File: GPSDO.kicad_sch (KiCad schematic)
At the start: 91 parts, among them J1 Conn_Coaxial, J10 PROG, J2 GPS_CONN, J3 Conn_Coaxial, J4 Conn_Coaxial, J5 Conn_Coaxial, J6 Conn_Coaxial, J7 DISP_MODULE, J8 Barrel_Jack, J9 Conn_Coaxial, SW1 RESET_BTN, U1 REF3450, U10 MC7805BDTRKG, U11 74AUC1G74, U12 74AUC2G04, U13 74AUC2G04, U14 DS34C87T, U15 MCP6486T-E/OT, U2 74LVC1G125SE-7, U3 AD5680, U4 NB3N551MN, U5 LTC2050IS8, U6 AVR32DB28x-xSO, U7 74LVC1G125SE-7, U8 74HC390, U9 L7805CV, X1 OC5SC25

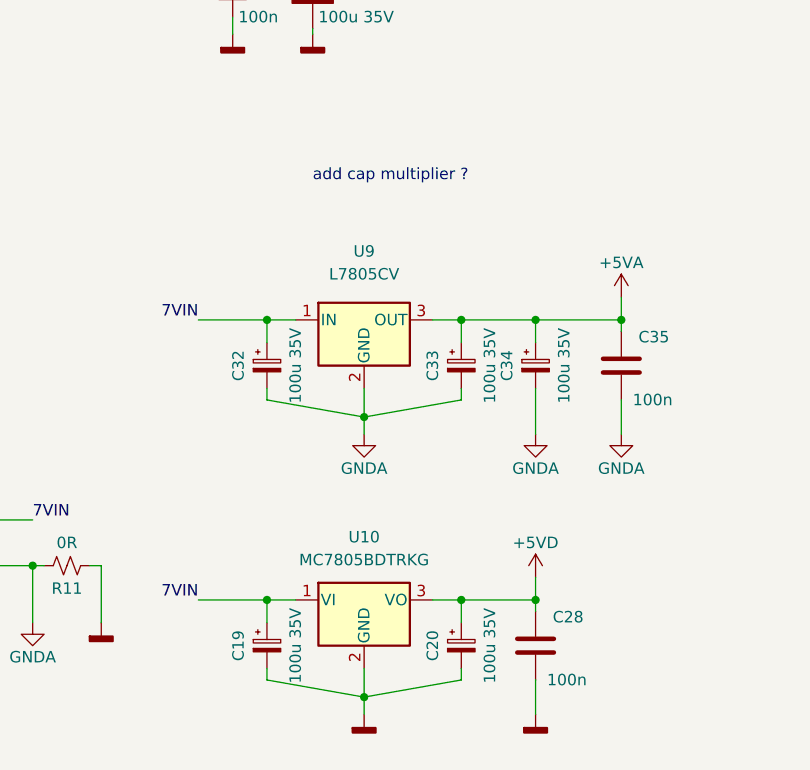
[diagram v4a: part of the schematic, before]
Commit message: LDO power supply
preliminary component choice
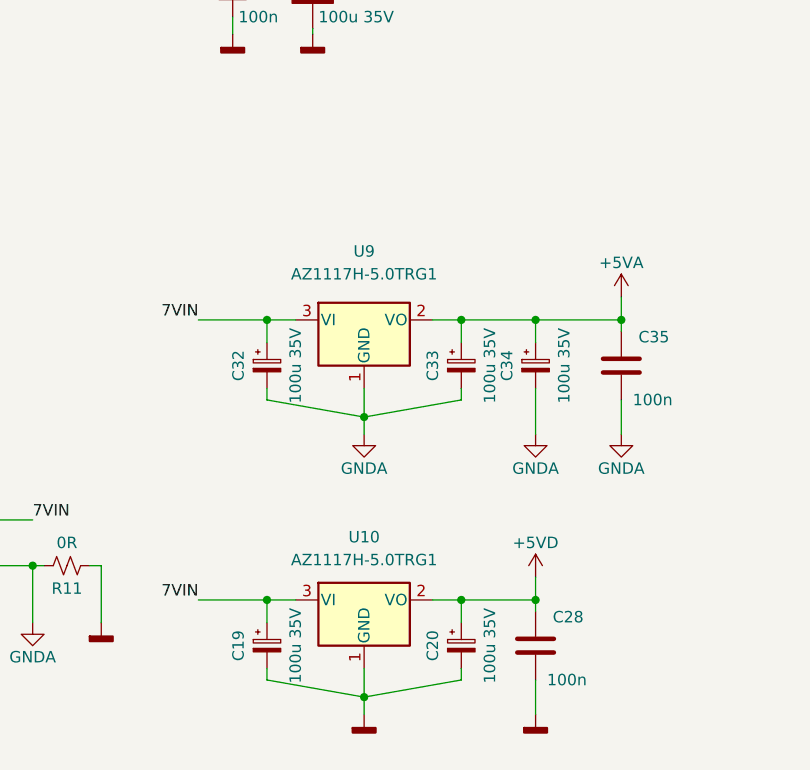
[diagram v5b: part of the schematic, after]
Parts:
- removed U10: MC7805BDTRKG, Package_TO_SOT_SMD:TO-252-2, symbol Regulator_Linear:LM78M05_TO252
- removed U9: L7805CV, Package_TO_SOT_THT:TO-220-3_Horizontal_TabDown, symbol Regulator_Linear:L7805
- added U10, U9: AZ1117H-5.0TRG1, Package_TO_SOT_SMD:SOT-223-3_TabPin2, symbol Regulator_Linear:AZ1117-5.0
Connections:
- net +5VA: now also U9.2 (VO)
- net +5VD: now also U10.2 (VO)
- net 7VIN: now also U10.3 (VI), U9.3 (VI)
- net GND: now also U10.1 (GND)
- net GNDA: now also U9.1 (GND)
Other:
- note removed: "add cap multiplier ?"
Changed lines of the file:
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@@
     (effects (font (size 1.27 1.27)) (justify left bottom))
   )
-  (text "add cap multiplier ?" (at 210.82 219.71 0)
-    (effects (font (size 1.27 1.27)) (justify left bottom))
-  )
   (text "TODO:\n - where to put trigger pin?\n - where to put ADC pin?\n-clock gen pow supply\n- check everything ok opn 5V?\n\n- (touch) display\n- serial interface\n- Main_clk_1 unused"
     (at 363.855 243.84 0)
@@
     (pin "1")
   )
-  (symbol (lib_id "Regulator_Linear:L7805") (at 216.535 234.95 0) (unit 1)
-    (in_bom yes) (on_board yes) (fields_autoplaced)
-    (property "Reference" "U9" (id 0) (at 216.535 227.33 0))
-    (property "Value" "L7805CV" (id 1) (at 216.535 229.87 0))
-    (property "Footprint" "Package_TO_SOT_THT:TO-220-3_Horizontal_TabDown" (id 2) (at 217.17 238.76 0)
-      (effects (font (size 1.27 1.27) italic) (justify left) hide)
-    )
-    (property "Datasheet" "http://www.st.com/content/ccc/resource/technical/document/datasheet/41/4f/b3/b0/12/d4/47/88/CD00000444.pdf/files/CD00000444.pdf/jcr:content/translations/en.CD00000444.pdf" (id 3) (at 216.535 236.22 0)
-      (effects (font (size 1.27 1.27)) hide)
-    )
-    (pin "1")
-    (pin "2")
-    (pin "3")
-  )
   (symbol (lib_id "power:GNDD") (at 93.345 113.03 0) (unit 1)
     (in_bom yes) (on_board yes) (fields_autoplaced)
@@
     (pin "1")
   )
+  (symbol (lib_id "Regulator_Linear:AZ1117-5.0") (at 216.535 234.95 0) (unit 1)
+    (in_bom yes) (on_board yes) (fields_autoplaced)
+    (property "Reference" "U9" (id 0) (at 216.535 227.33 0))
+    (property "Value" "AZ1117H-5.0TRG1" (id 1) (at 216.535 229.87 0))
+    (property "Footprint" "Package_TO_SOT_SMD:SOT-223-3_TabPin2" (id 2) (at 216.535 228.6 0)
+      (effects (font (size 1.27 1.27) italic) hide)
+    )
+    (property "Datasheet" "https://www.diodes.com/assets/Datasheets/AZ1117.pdf" (id 3) (at 216.535 234.95 0)
+      (effects (font (size 1.27 1.27)) hide)
+    )
+    (pin "1")
+    (pin "2")
+    (pin "3")
+  )
   (symbol (lib_id "power:GNDD") (at 53.975 273.05 0) (unit 1)
     (in_bom yes) (on_board yes) (fields_autoplaced)
@@
     (pin "2")
   )
-  (symbol (lib_id "Regulator_Linear:LM78M05_TO252") (at 216.535 266.065 0) (unit 1)
-    (in_bom yes) (on_board yes) (fields_autoplaced)
-    (property "Reference" "U10" (id 0) (at 216.535 259.08 0))
-    (property "Value" "MC7805BDTRKG" (id 1) (at 216.535 261.62 0))
-    (property "Footprint" "Package_TO_SOT_SMD:TO-252-2" (id 2) (at 216.535 260.35 0)
-      (effects (font (size 1.27 1.27) italic) hide)
-    )
-    (property "Datasheet" "https://www.onsemi.com/pub/Collateral/MC78M00-D.PDF" (id 3) (at 216.535 267.335 0)
-      (effects (font (size 1.27 1.27)) hide)
-    )
-    (pin "1")
-    (pin "2")
-    (pin "3")
-  )
   (symbol (lib_id "Device:C_Polarized") (at 20.955 267.97 0) (unit 1)
     (in_bom yes) (on_board yes)
@@
     (pin "1")
   )
+  (symbol (lib_id "Regulator_Linear:AZ1117-5.0") (at 216.535 266.065 0) (unit 1)
+    (in_bom yes) (on_board yes) (fields_autoplaced)
+    (property "Reference" "U10" (id 0) (at 216.535 259.08 0))
+    (property "Value" "AZ1117H-5.0TRG1" (id 1) (at 216.535 261.62 0))
+    (property "Footprint" "Package_TO_SOT_SMD:SOT-223-3_TabPin2" (id 2) (at 216.535 259.715 0)
+      (effects (font (size 1.27 1.27) italic) hide)
+    )
+    (property "Datasheet" "https://www.diodes.com/assets/Datasheets/AZ1117.pdf" (id 3) (at 216.535 266.065 0)
+      (effects (font (size 1.27 1.27)) hide)
+    )
+    (pin "1")
+    (pin "2")
+    (pin "3")
+  )
   (symbol (lib_id "power:+5VD") (at 44.45 262.255 0) (unit 1)
     (in_bom yes) (on_board yes) (fields_autoplaced)
@@
       (reference "U8") (unit 3) (value "74HC390") (footprint "Package_SO:SOIC-16_3.9x9.9mm_P1.27mm")
     )
-    (path "/171f434d-5c34-48ea-8f79-c330c808a2be"
-      (reference "U9") (unit 1) (value "L7805CV") (footprint "Package_TO_SOT_THT:TO-220-3_Horizontal_TabDown")
+    (path "/503e0e75-e692-4d20-8364-7dd959ad220a"
+      (reference "U9") (unit 1) (value "AZ1117H-5.0TRG1") (footprint "Package_TO_SOT_SMD:SOT-223-3_TabPin2")
     )
-    (path "/89b8a5aa-f785-4e60-9e1c-9f4b79a3f39c"
-      (reference "U10") (unit 1) (value "MC7805BDTRKG") (footprint "Package_TO_SOT_SMD:TO-252-2")
+    (path "/e6bc66eb-279a-48bf-9d76-c75432f12fc9"
+      (reference "U10") (unit 1) (value "AZ1117H-5.0TRG1") (footprint "Package_TO_SOT_SMD:SOT-223-3_TabPin2")
     )
     (path "/14b7ea0b-a3fe-410e-b47a-552eaf1c5ffd"

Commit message: minor update
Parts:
- removed C10: 100u 35V, Capacitor_SMD:C_Elec_6.3x7.7, symbol Device:C_Polarized
- added D3: LED, LED_SMD:LED_0805_2012Metric, symbol Device:LED
- added R13: 270R, Resistor_SMD:R_0805_2012Metric_Pad1.20x1.40mm_HandSolder, symbol Device:R_Small_US
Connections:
- net +5VA: now also D3.2 (A)
- net GNDA: now also R13.1
- new net: D3.1 (K), R13.2
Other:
- note added: "PD4 is the Waveform Output for TCA0"
- moved on the sheet: C31, C46, J10, J2, J9, R12, R8, R9, U11, U15, U2, U7

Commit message: intermediate solution for layout
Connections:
- net TOUCH_IRQ: now also U6.1 (PA7); no longer U6.8 (PD2)
- net ~{DAC_SS}: now also U6.8 (PD2); no longer U6.1 (PA7)
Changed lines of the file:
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@@
     (effects (font (size 1.27 1.27)) (justify right bottom))
   )
-  (label "TOUCH_IRQ" (at 151.13 111.76 0)
-    (effects (font (size 1.27 1.27)) (justify left bottom))
+  (label "TOUCH_IRQ" (at 217.805 111.76 180)
+    (effects (font (size 1.27 1.27)) (justify right bottom))
   )
   (label "~{TOUCH_SS}" (at 217.805 124.46 180)
@@
     (effects (font (size 1.27 1.27)) (justify left bottom))
   )
-  (label "~{DAC_SS}" (at 217.805 111.76 180)
-    (effects (font (size 1.27 1.27)) (justify right bottom))
+  (label "~{DAC_SS}" (at 151.13 111.76 0)
+    (effects (font (size 1.27 1.27)) (justify left bottom))
   )
   (label "TOUCH_MISO" (at 231.775 119.38 180)

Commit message: first routing
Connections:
- net GND: now also R11.2; no longer R11.1
- net GNDA: now also R11.1; no longer R11.2
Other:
- note added: "DAC and LCD Touch share SPI iface"
- moved on the sheet: R11
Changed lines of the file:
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@@
+    (effects (font (size 1.27 1.27)) (justify left bottom))
+  )
+  (text "DAC and LCD Touch share\nSPI iface" (at 243.84 120.65 0)
     (effects (font (size 1.27 1.27)) (justify left bottom))
   )
@@
     (pin "1")
   )
-  (symbol (lib_id "Device:R_Small_US") (at 183.515 262.255 270) (unit 1)
+  (symbol (lib_id "Device:R_Small_US") (at 183.515 262.255 90) (mirror x) (unit 1)
     (in_bom yes) (on_board yes)
     (property "Reference" "R11" (id 0) (at 183.515 264.795 90))
